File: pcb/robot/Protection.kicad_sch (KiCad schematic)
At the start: 46 parts, among them IC1 TPS22998RYZR, Q2 EFC8811R-TF, Q7 Q_NMOS_GDS, SW1 SW_SPST, U12 BQ27742YZFR-G1

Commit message: Re-unify USB-PD module into main board (single-PCB architecture) (#17)
Merges the USB-PD module circuitry back into the main robot board as
a single PCB, reversing the earlier main-board/USB-PD-daughter-board
split. Full re-route and re-placement of the combined design:

- Consolidated low-profile parts toward the board center, using the
  space freed up by relocated capacitors, for better overall use of
  the available area.
- Kept all 0-ohm test/isolation jumpers in accessible locations for
  bench testing.
- Added/corrected footprints for several parts that had broken or
  incorrect footprints (DDC6_TEX variants, SOT-23-6, SOT-23-3,
  R0402).

Carries forward every closed correction issue and update made since
the original split: #3 (CC jumpers), #6 (IC1.ON pull-down), #14/#15
(ADC divider, motor connector pinout), #16, #18 (I2C isolation
jumpers), #19 (charger-sense GPIO interrupt), plus the BOM/pricing
updates, LED changes, and MAX77642 replacement.

Verified via kicad-cli ERC/DRC + netlist diff against the pre-merge
board: 0 unconnected items (unchanged), no new DRC error-level
violations besides one pre-existing excluded item, and the #6
(IC1.ON pull-down) and #19 (charger-sense GPIO interrupt) circuits
confirmed intact at the net-topology level despite the full-board
re-annotation changing most reference designators. Most of the raw
diff size is a KiCad 9 footprint-format upgrade (pre-2023 format
rewritten to current) rather than design changes - spot-checked
against unrelated footprints (e.g. mounting holes), which show
identical geometry under the new syntax.
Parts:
- NT11: renamed from NT13; symbol Device:NetTie_2 -> robot:NetTie_2
- NT12: renamed from NT10; symbol Device:NetTie_2 -> robot:NetTie_2
- NT13: renamed from NT12; symbol Device:NetTie_2 -> robot:NetTie_2
- NT15: renamed from NT9; symbol Device:NetTie_2 -> robot:NetTie_2
- NT16: renamed from NT8; symbol Device:NetTie_2 -> robot:NetTie_2
- NT17: renamed from NT7; symbol Device:NetTie_2 -> robot:NetTie_2
- R73: renamed from R34; symbol Device:R -> robot:R
- R74: renamed from R35; symbol Device:R -> robot:R
- R82: renamed from R13; symbol easyeda2kicad:0402WGJ0474TCE -> robot:0402WGJ0474TCE
- renumbered BT2 to BT1, BT1 to BT2, C55 to C34, C57 to C35, C56 to C36, C58 to C37, C59 to C42, C60 to C44, C61 to C45, C62 to C47, C63 to C49, C64 to C50, C65 to C53, C66 to C54, C96 to C56, C106 to C58, C107 to C59, C108 to C60, Q7 to Q4, Q2 to Q5, R41 to R67, R42 to R68, R43 to R75, R44 to R76, R45 to R77, R8 to R78, R46 to R79, R47 to R80, R48 to R81, S1 to S3, TP28 to TP26, U12 to U22

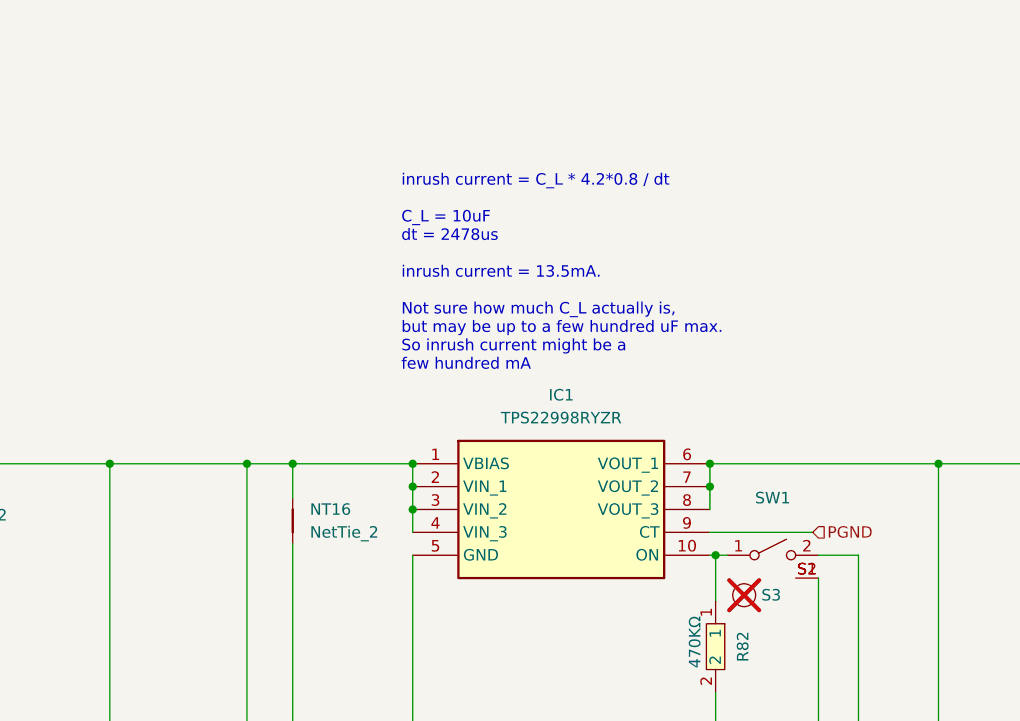
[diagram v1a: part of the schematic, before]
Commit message: Add switch-open discharge detector and low-power OV reference (#22, #23)
U34 (new, MCP6541 on IC1-VBIAS) senses the power switch via
Net-(IC1-ON) and forces Q7/R124 (#22's shunt) to discharge
/MOTORS/VCC when the switch opens, independent of the 3V3 rail.
OR'd into Q7's gate through D11/D12 alongside U32's existing
overvoltage trip - discharges in ~2.2ms vs. the ~500-600ms the
MAX77857 was timing out at.

Also swaps U33 (TLVH431) for a MAX6006A micropower reference and
bumps R131 to 412k, per Christopher's request on #22 - cuts the
clamp's standing current from ~218uA to ~18uA with the same
5.6V/5.4V thresholds.

Verified with kicad-cli: ERC clean, 0 unconnected items, schematic
parity clean (pre-existing U12 footprint mismatch aside).
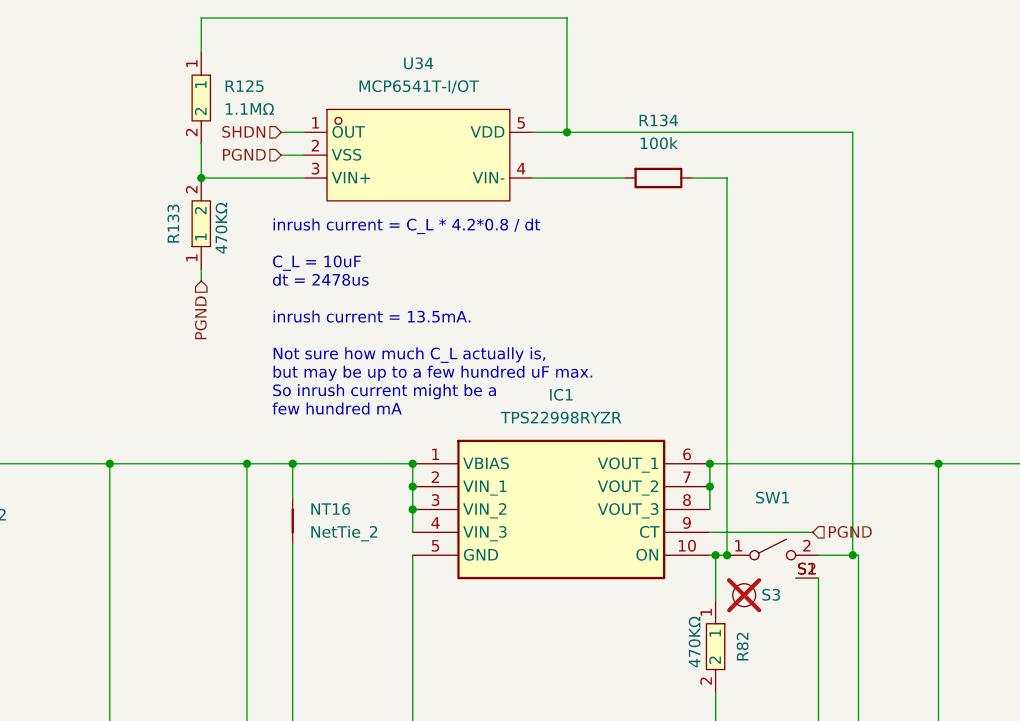
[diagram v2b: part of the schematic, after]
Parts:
- added R125: 1.1MΩ, easyeda2kicad:R0402, symbol easyeda2kicad:0402WGF1104TCE
- added R133: 0402WGJ0474TCE, easyeda2kicad:R0402, symbol robot:0402WGJ0474TCE
- added R134: 100k, robot:R_0402_1005Metric, symbol robot:R
- added U34: MCP6541T-I/OT, easyeda2kicad:SOT-23-5_L3.0-W1.7-P0.95-LS2.8-BR, symbol easyeda2kicad:MCP6541T-I_OT
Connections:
- net PGND: now also R133.1, U34.2 (VSS)
- net at NT16.2, SW1.2 (B): now also R125.1, U34.5 (VDD)
- net at IC1.10 (ON), R82.1, SW1.1 (A): now also R134.1
- new net: R125.2, R133.2, U34.3 (VIN+)
- new net: R134.2, U34.4 (VIN-)
- new net SHDN: U34.1 (OUT)

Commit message: Clean up BOM fields, regenerate gerbers/BOM/CPL for fab order (#17)
MPN -> Part Number field rename on a few parts in Protection.kicad_sch
and USB-PD-PhonePC.kicad_sch for consistent BOM output. R48 value
0 -> S0 (it's the 3-pin switch footprint, not a real resistor value).
Re-exported gerbers, drill files, BOM and CPL for the JLCPCB
fab+assembly order just placed.
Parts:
- R125: MPN 0402WGF1104TCE -> (none); Part Number (none) -> 0402WGF1104TCE
- U34: MPN MCP6541T-I/OT -> (none); Part Number (none) -> MCP6541T-I/OT
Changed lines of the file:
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@@
 			)
 		)
-		(property "MPN" "MCP6541T-I/OT"
+		(property "Part Number" "MCP6541T-I/OT"
 			(at 283.21 64.77 0)
 			(effects
@@
 			)
 		)
-		(property "MPN" "0402WGF1104TCE"
+		(property "Part Number" "0402WGF1104TCE"
 			(at 243.84 40.64 0)
 			(effects
